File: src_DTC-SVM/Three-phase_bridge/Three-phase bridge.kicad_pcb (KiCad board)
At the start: 2 copper layers, 412.2 x 322.6 mm, 94 parts, among them M1 MCP6022-I/P, M2 MCP6022-I/P, P1 CONN_1, P2 POWER_FUSE, P3 CONN_2, P4 CONN_1, P5 CONN_1, P6 POWER_FUSE, P7 CONN_1, P8 CONN_1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

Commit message: PCB: Module T0-220 has been modified so that pin number 4 (for heat sink) is electrically connected to pin 3 (drain). Now whe the fill zones are filled, the heatsinks are connected to the PCB dissipation area. As consequence, SVG files were regenerated.
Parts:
- S1, S2, S3, S4, S5, S6: footprint TO220_Big_Heat_Sink -> TO220_Big_Heat_Sink_Drain_Sink
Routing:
- added copper zone on F.Cu, net N-000008
- added copper zone on F.Cu, net N-0000082
- removed copper zone on F.Cu, net N-0000070
- removed copper zone on F.Cu, net N-000009

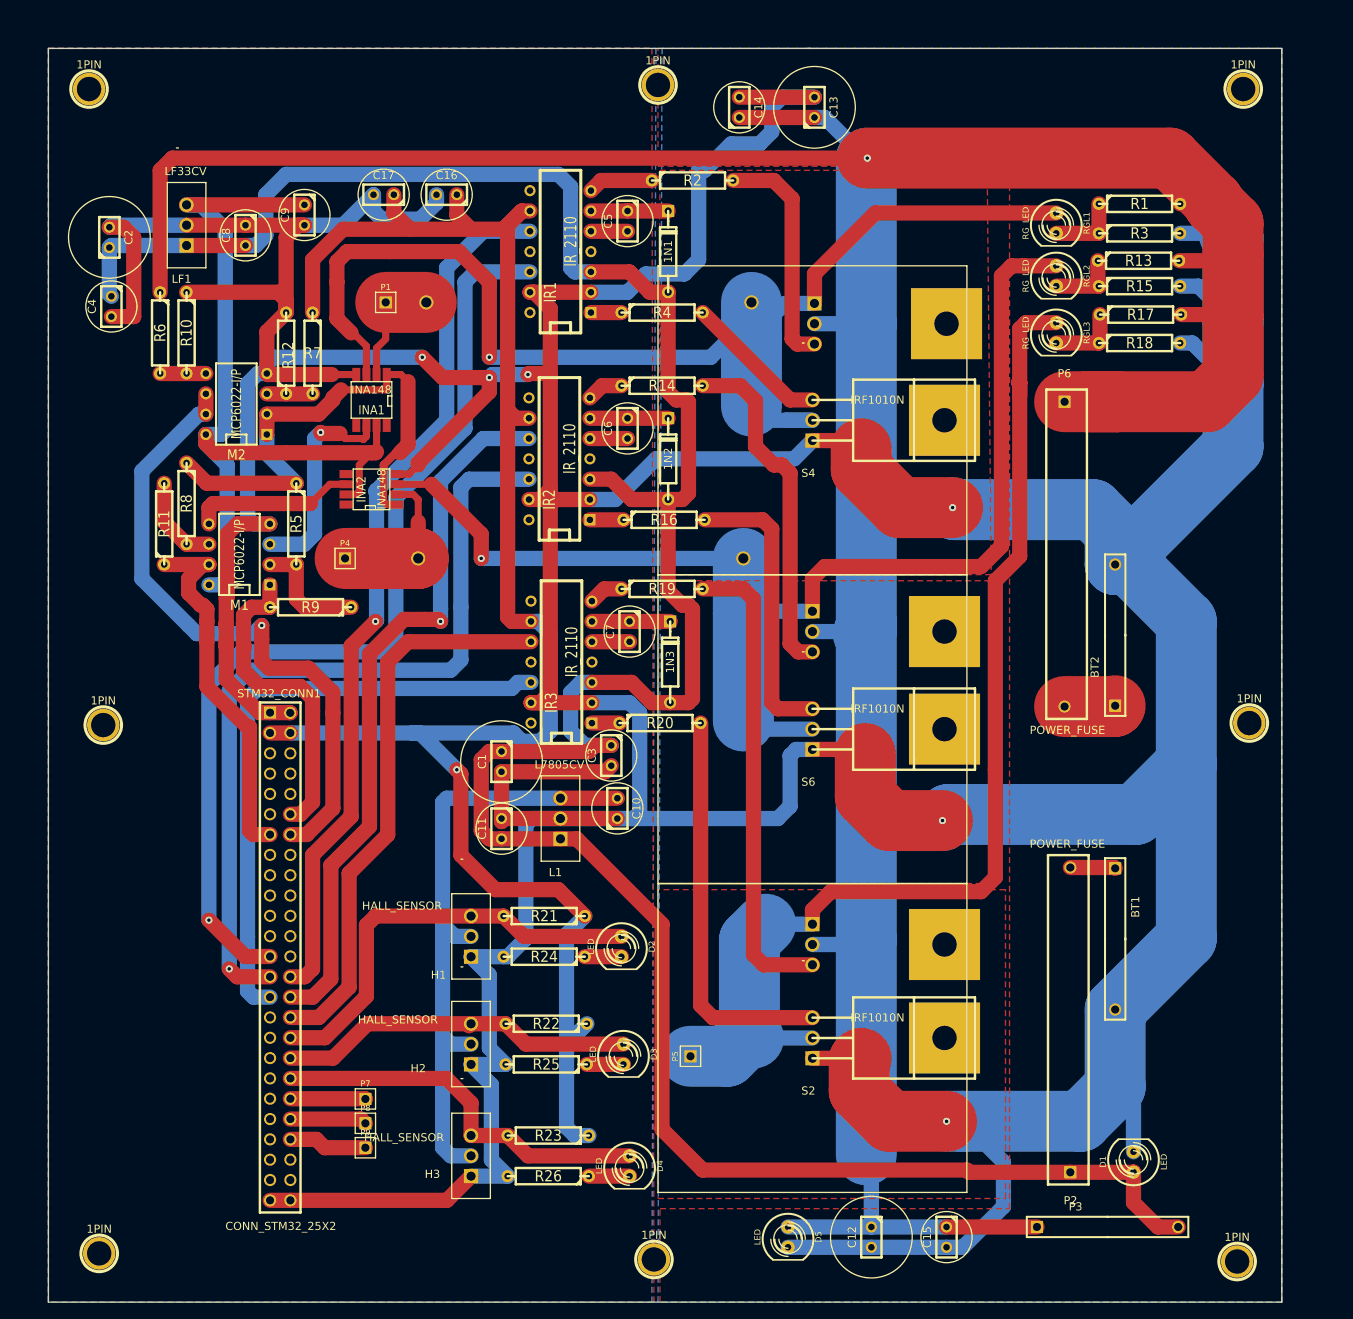
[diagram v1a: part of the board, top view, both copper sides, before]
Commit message: PCB: Some capacitor were moved in order to reduce the final PCBarea. Now it is 5.80in x5.72in.
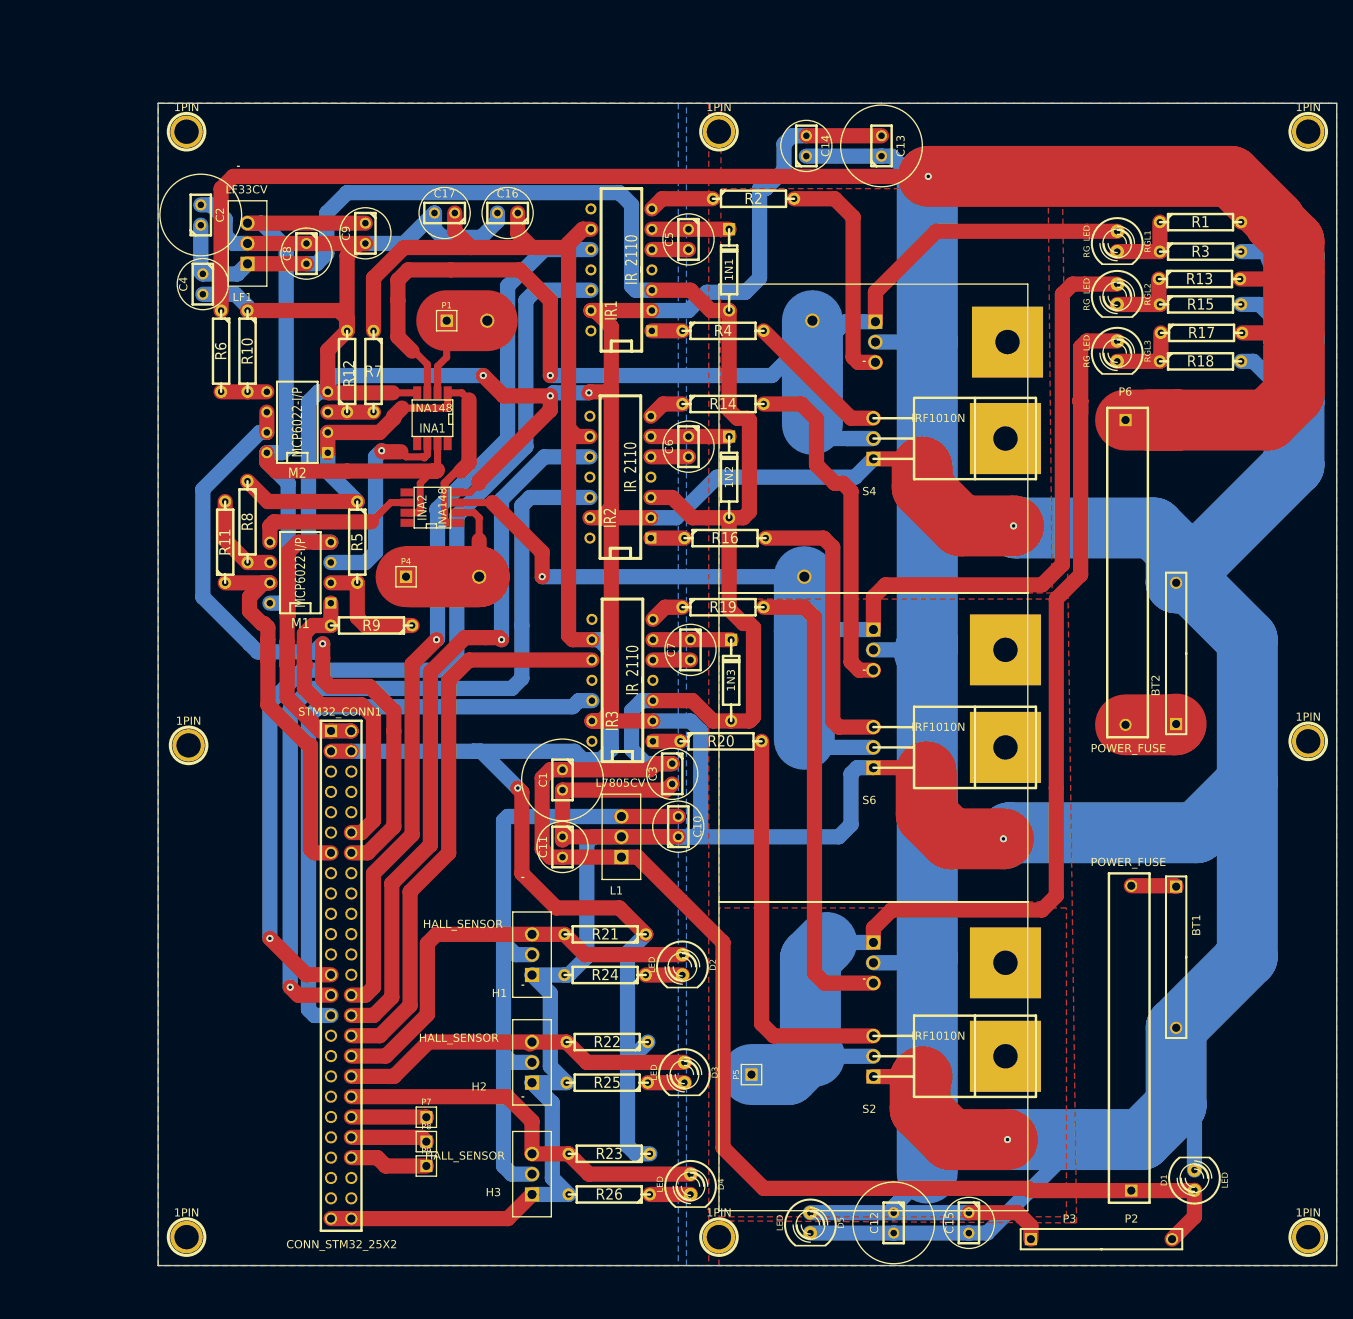
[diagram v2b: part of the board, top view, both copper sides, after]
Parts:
- moved 1PIN 13.3 mm to (149.6, 68.1)
- moved C4 11.8 mm to (151.6, 87.1)
- moved C2 11.8 mm to (151.4, 78.5)
- moved 1PIN 11.1 mm to (149.6, 206.2)
- moved 1PIN 11.0 mm to (149.9, 144.8)
- moved 1PIN 9.72 mm to (289.8, 68.1)
- moved C14 9.67 mm to (227.1, 69.8)
- moved C13 9.67 mm to (236.5, 69.8)
- moved 1PIN 9.60 mm to (216.2, 68.1)
- moved 1PIN 9.40 mm to (289.8, 206.2)
- moved 1PIN 8.59 mm to (216.2, 206.2)
- moved R9 7.96 mm to (172.7, 129.8)
- moved 1N2 7.96 mm to (217.4, 111.3)
- moved C1 7.96 mm to (196.6, 149.1)
- moved C10 7.96 mm to (211.1, 154.9)
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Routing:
- net GND: track 924.2 -> 901.2 mm
- net VCC: track 340.6 -> 333.5 mm
- net +48V: track 426.7 -> 422.0 mm
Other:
- board size 412.2 x 322.6 mm -> 419.1 x 318 mm
